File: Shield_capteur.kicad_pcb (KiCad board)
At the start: 2 copper layers, 68.6 x 53.3 mm, 16 parts, among them J1 Power, J2 Digital/PWM, J3 Analog, J4 Digital/PWM

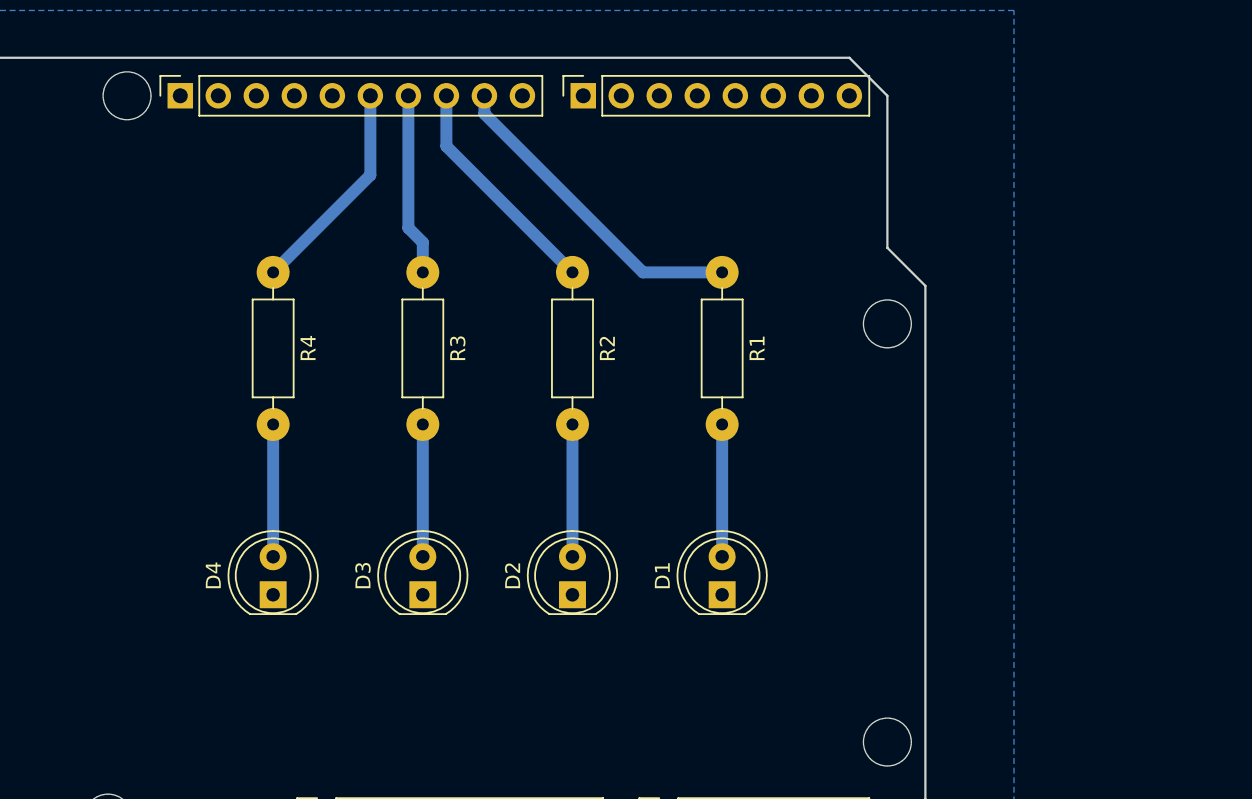
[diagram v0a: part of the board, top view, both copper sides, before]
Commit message: Avancée sur le shield, schéma +footprint
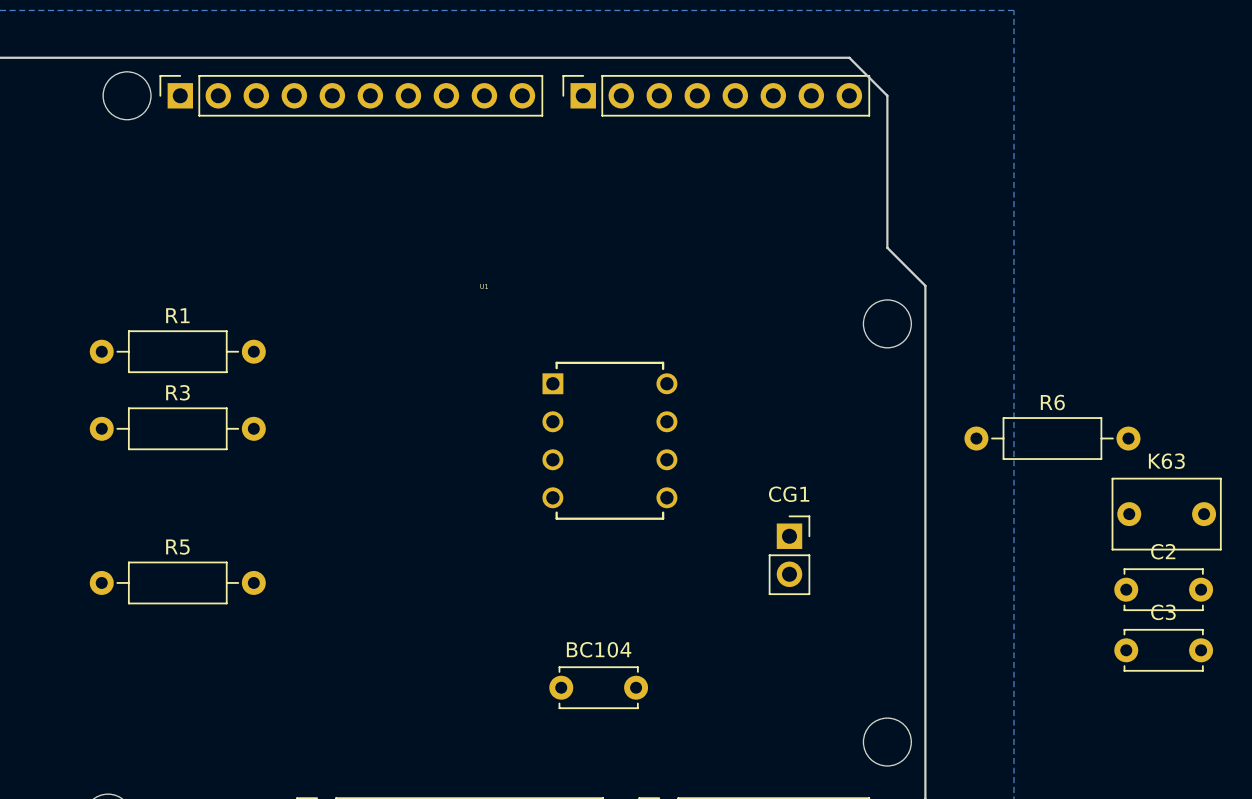
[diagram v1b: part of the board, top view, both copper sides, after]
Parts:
- removed D1, D2, D3, D4: LED, LED_THT:LED_D5.0mm
- removed R2, R4: R, Resistor_THT:R_Axial_DIN0207_L6.3mm_D2.5mm_P10.16mm_Horizontal
- added BC104: 100nF, Capacitor_THT:C_Disc_D5.0mm_W2.5mm_P5.00mm, F.Cu at (144.2, 88.8)
- added C2: BC104, Capacitor_THT:C_Disc_D5.0mm_W2.5mm_P5.00mm, F.Cu at (182.0, 82.2)
- added C3: BC104, Capacitor_THT:C_Disc_D5.0mm_W2.5mm_P5.00mm, F.Cu at (182.0, 86.2)
- added CG1: ~, Connector_PinSocket_2.54mm:PinSocket_1x02_P2.54mm_Vertical, F.Cu at (159.5, 78.6)
- added K63: 1uF, Capacitor_THT:C_Rect_L7.0mm_W4.5mm_P5.00mm, F.Cu at (182.2, 77.2)
- added R5: 10k, Resistor_THT:R_Axial_DIN0207_L6.3mm_D2.5mm_P10.16mm_Horizontal, F.Cu at (113.5, 81.8)
- added R6: 1k, Resistor_THT:R_Axial_DIN0207_L6.3mm_D2.5mm_P10.16mm_Horizontal, F.Cu at (172.0, 72.1)
- added U1: LTC1050ACN8_PBF, LTC1050ACN8_PBF:PDIP-8_N, F.Cu at (151.3, 76.1)
- R1, R3: value R -> 100k
- moved R1 41.8 mm to (113.5, 66.3), turned to 0 degrees
- moved R3 23.9 mm to (113.5, 71.5), turned to 0 degrees
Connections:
- R1 pad 1: /LED_D9 -> unconnected-(R1-Pad1)
- R1 pad 2: Net-(D1-A) -> unconnected-(R1-Pad2)
- R3 pad 1: /LED_D11 -> unconnected-(R3-Pad1)
- R3 pad 2: Net-(D3-A) -> unconnected-(R3-Pad2)
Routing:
- net /LED_D9: track 21.5 -> 0.00 mm
- net /LED_D10: track 15.3 -> 0.00 mm
- net /LED_D12: track 14.5 -> 0.00 mm
- net /LED_D11: track 12.2 -> 0.00 mm
- net Net-(D4-A): track 8.84 -> 0.00 mm
- net Net-(D3-A): track 8.84 -> 0.00 mm
- net Net-(D2-A): track 8.84 -> 0.00 mm
- net Net-(D1-A): track 8.84 -> 0.00 mm

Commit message: Progrès TD Datasheet
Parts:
- added HC-1: ~, Connector_PinSocket_2.54mm:PinSocket_1x04_P2.54mm_Vertical, F.Cu at (183.1, 97.6)
- added U2: LTC1050ACN8_PBF, LTC1050ACN8_PBF:PDIP-8_N, F.Cu at (179.2, 58.3)
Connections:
- net /LED_D12 renamed /D12
- net /LED_D9 renamed /D9
- BC104 pad 1: unconnected-(BC104-Pad1) -> Net-(U1-+IN)
- BC104 pad 2: unconnected-(BC104-Pad2) -> GND
- C2 pad 1: unconnected-(C2-Pad1) -> /A0
- C2 pad 2: unconnected-(C2-Pad2) -> GND
- C3 pad 1: unconnected-(C3-Pad1) -> GND
- C3 pad 2: unconnected-(C3-Pad2) -> VCC
- CG1 pad 1: unconnected-(CG1-Pad1) -> VCC
- CG1 pad 2: unconnected-(CG1-Pad2) -> Net-(CG1-Pad2)
- J2 pad 5: /13 -> /D13
- J2 pad 7: /LED_D11 -> /D11
- J2 pad 8: /LED_D10 -> /D10
- K63 pad 1: unconnected-(K63-Pad1) -> Net-(U1--IN)
- K63 pad 2: unconnected-(K63-Pad2) -> Net-(U1-OUT)
- R1 pad 1: unconnected-(R1-Pad1) -> Net-(U1-+IN)
- R1 pad 2: unconnected-(R1-Pad2) -> GND
- R3 pad 1: unconnected-(R3-Pad1) -> Net-(U1--IN)
- R3 pad 2: unconnected-(R3-Pad2) -> Net-(U1-OUT)
- R5 pad 1: unconnected-(R5-Pad1) -> Net-(CG1-Pad2)
- R5 pad 2: unconnected-(R5-Pad2) -> Net-(U1-+IN)
- R6 pad 1: unconnected-(R6-Pad1) -> /A0
- R6 pad 2: unconnected-(R6-Pad2) -> Net-(U1-OUT)
- U1 pad 2: unconnected-(U1--IN-Pad2) -> Net-(U1--IN)
- U1 pad 3: unconnected-(U1-+IN-Pad3) -> Net-(U1-+IN)
- U1 pad 4: unconnected-(U1-V--Pad4) -> GND
- U1 pad 6: unconnected-(U1-OUT-Pad6) -> Net-(U1-OUT)
- U1 pad 7: unconnected-(U1-V+-Pad7) -> VCC

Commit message: Fin de la schematic
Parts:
- added B1: ~, New_bouton:Boutons_x3, F.Cu at (199.1, 65.6)
- added Flex: ~, Connector_PinSocket_2.54mm:PinSocket_1x02_P2.54mm_Vertical, F.Cu at (219.5, 78.7)
- added U3: ~, Connector_PinSocket_2.54mm:PinSocket_1x04_P2.54mm_Vertical, F.Cu at (211.2, 28.7)
- moved HC-1 83.5 mm to (103.0, 74.0)
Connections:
- HC-1 pad 1: (no net) -> VCC
- HC-1 pad 2: (no net) -> GND
- HC-1 pad 3: (no net) -> /D7
- HC-1 pad 4: (no net) -> /D8
- J2 pad 10: unconnected-(J2-Pin_10-Pad10) -> /D8
- J4 pad 1: /7 -> /D7
- J4 pad 4: /4 -> /D4
- J4 pad 6: /2 -> /D2
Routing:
- added copper zone on B.Cu, net GND
- removed copper zone on B.Cu, net (none)

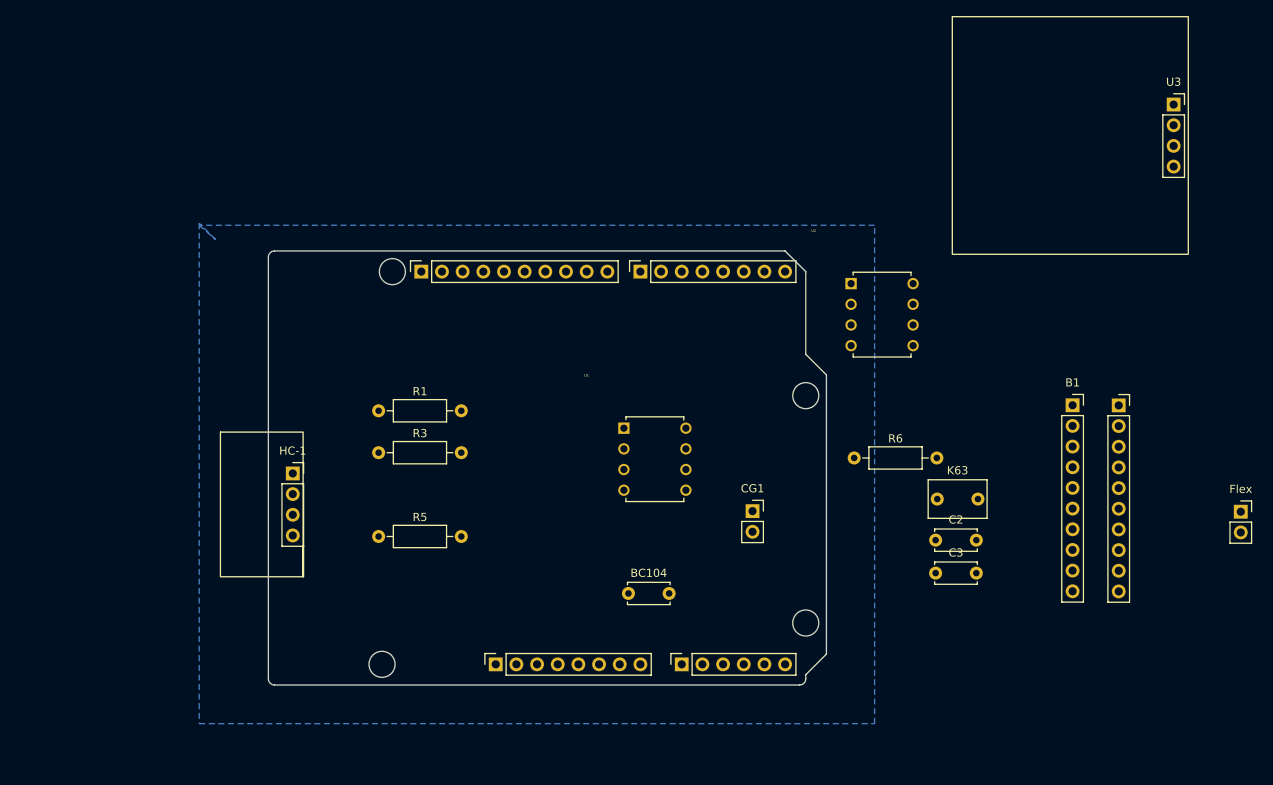
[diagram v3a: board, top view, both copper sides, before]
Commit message: Changement pastilles PCB
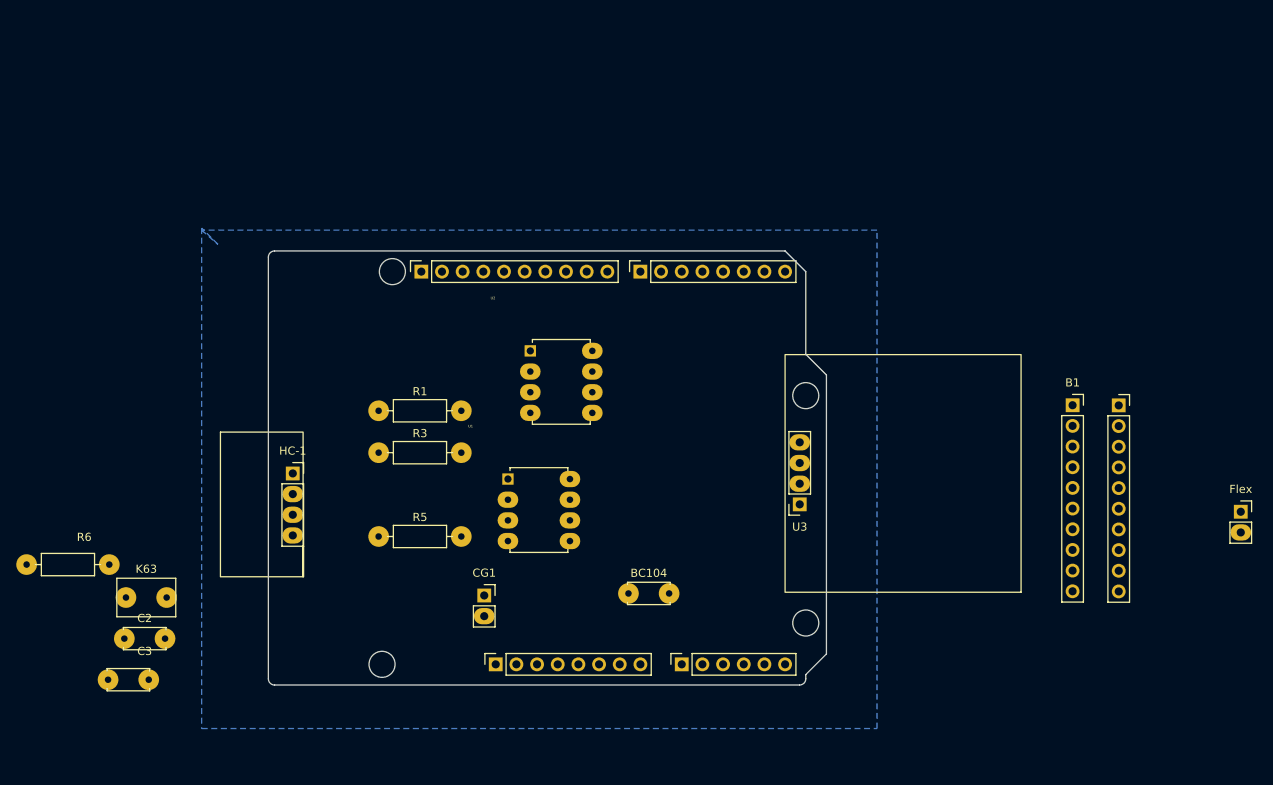
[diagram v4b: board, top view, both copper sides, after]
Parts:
- moved C3 102.5 mm to (80.3, 99.3)
- moved R6 102.5 mm to (70.3, 85.2)
- moved C2 100.4 mm to (82.3, 94.3)
- moved K63 100.4 mm to (82.5, 89.2)
- moved U3 67.3 mm to (165.3, 77.8), turned to 180 degrees
- moved U2 40.3 mm to (139.8, 66.6)
- moved CG1 34.6 mm to (126.5, 89.0)
- moved U1 15.6 mm to (137.1, 82.3)

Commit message: Avancé PCB positionnement de tous les composants
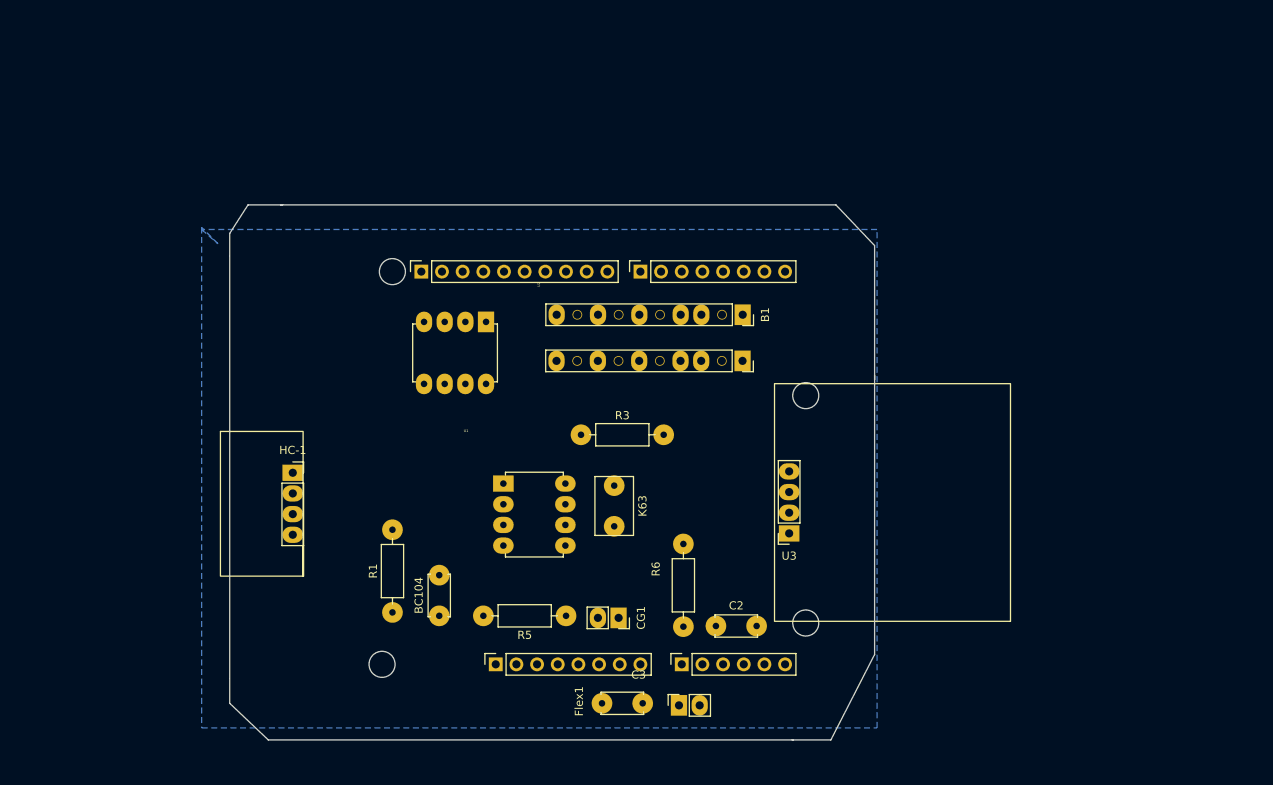
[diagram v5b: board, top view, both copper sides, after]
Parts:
- U2: value LTC1050ACN8_PBF -> MCP
- moved R6 81.1 mm to (151.0, 92.8), turned to 90 degrees
- moved Flex1 73.0 mm to (150.5, 102.5), turned to 90 degrees
- moved C2 72.7 mm to (155.0, 92.8)
- moved K63 61.6 mm to (142.5, 75.5), turned to -90 degrees
- moved C3 60.8 mm to (141.0, 102.2)
- moved B1 42.2 mm to (158.3, 54.8), turned to -90 degrees
- moved R5 25.0 mm to (136.6, 91.5), turned to 180 degrees
- moved R3 25.0 mm to (138.4, 69.2)
- moved R1 24.8 mm to (115.2, 91.1), turned to 90 degrees
- moved BC104 23.4 mm to (121.0, 91.5), turned to 90 degrees
- moved U2 21.0 mm to (119.1, 63.0), turned to -90 degrees
- moved CG1 16.7 mm to (143.0, 91.8), turned to -90 degrees
- moved U3 3.80 mm to (164.0, 81.4)
- moved U1 0.79 mm to (136.5, 82.9)
- moved HC-1 0.08 mm to (103.0, 73.9)
- renumbered Flex to Flex1
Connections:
- B1 pad 10: (no net) -> GND
- B1 pad 2: GND -> (no net)
- B1 pad 3: /D4 -> GND
- B1 pad 4: GND -> /D4
- B1 pad 5: /D12 -> (no net)
- B1 pad 8: (no net) -> /D12
- Flex1 pad 1: (no net) -> VCC
- Flex1 pad 2: (no net) -> /A1
- U3 pad 1: (no net) -> GND
- U3 pad 2: (no net) -> VCC
- U3 pad 3: (no net) -> /SCL
- U3 pad 4: (no net) -> /SDA
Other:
- board size 68.6 x 53.3 mm -> 79.2 x 65.8 mm

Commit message: Fin du placement des composants et pistes sur PCB. Quelques erreurs mineures à régler
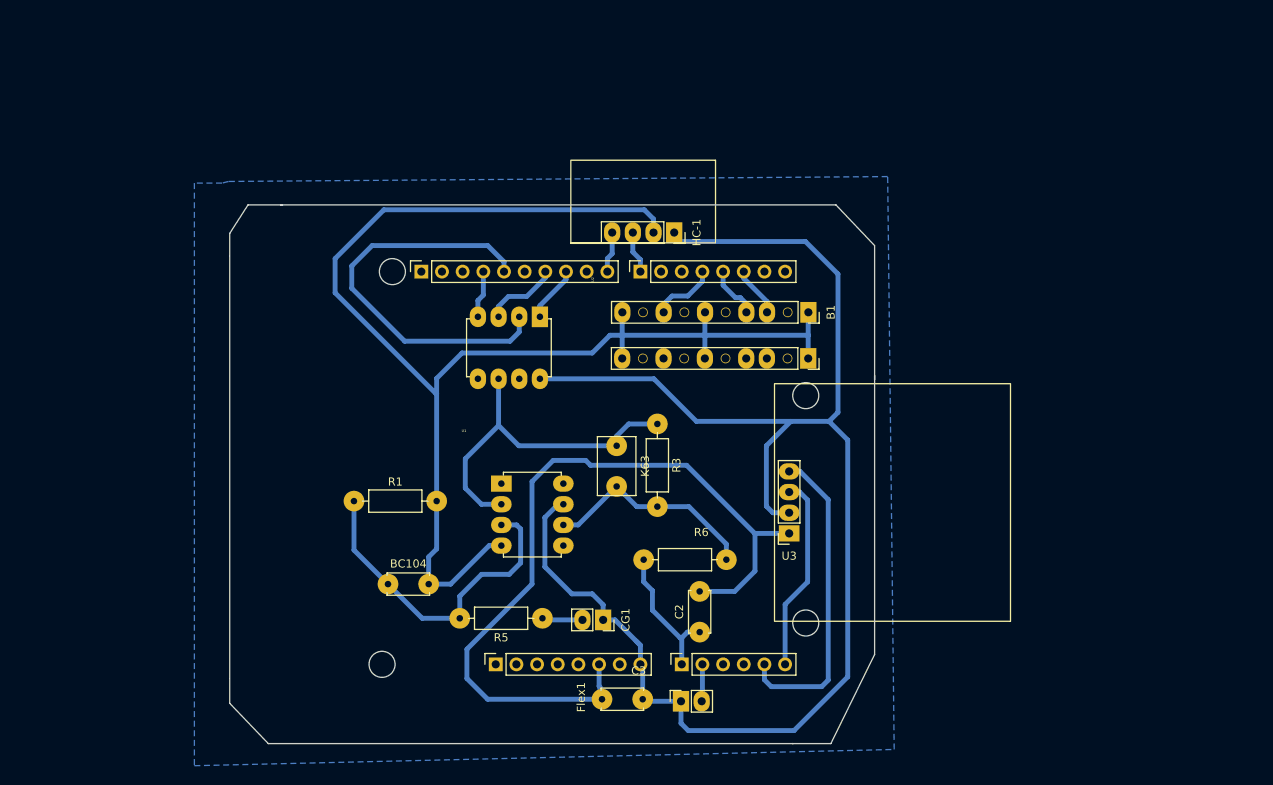
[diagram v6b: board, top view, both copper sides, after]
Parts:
- moved HC-1 55.4 mm to (149.9, 44.4), turned to -90 degrees
- moved R1 14.5 mm to (110.5, 77.4), turned to 0 degrees
- moved R6 9.57 mm to (146.1, 84.6), turned to 0 degrees
- moved R3 9.47 mm to (147.8, 67.9), turned to -90 degrees
- moved B1 8.08 mm to (166.4, 54.5)
- moved BC104 7.41 mm to (114.7, 87.6), turned to 0 degrees
- moved U2 6.65 mm to (125.8, 62.4)
- moved K63 4.91 mm to (142.8, 70.6)
- moved R5 2.92 mm to (133.7, 91.8)
- moved C2 2.14 mm to (153.0, 93.5), turned to 90 degrees
- moved CG1 1.92 mm to (141.1, 92.0)
- moved Flex1 0.56 mm to (150.7, 102.0)
- moved C3 0.50 mm to (141.0, 101.8)
- moved U1 0.25 mm to (136.2, 82.9)
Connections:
- B1 pad 1: /D2 -> GND
- B1 pad 3: GND -> /D2
- B1 pad 4: /D4 -> /*3
- B1 pad 8: /D12 -> /D4
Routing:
- net GND: track 0.00 -> 272.9 mm
- net VCC: track 0.00 -> 190.1 mm
- net /D13: track 0.00 -> 50.1 mm
- net Net-(U1--IN): track 0.00 -> 42.7 mm
- net Net-(U1-+IN): track 0.00 -> 41.1 mm
- net /SDA: track 0.00 -> 38.8 mm
- net Net-(U1-OUT): track 0.00 -> 26.8 mm
- net /SCL: track 0.00 -> 24.0 mm
- net /A0: track 0.00 -> 17.4 mm
- net /D11: track 0.00 -> 9.28 mm
- net /D4: track 0.00 -> 8.11 mm
- net /D10: track 0.00 -> 6.88 mm
- net /*3: track 0.00 -> 6.54 mm
- net /D2: track 0.00 -> 6.18 mm
- net Net-(CG1-Pad2): track 0.00 -> 5.00 mm
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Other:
- board size 79.2 x 65.8 mm -> 79.2 x 66.2 mm
